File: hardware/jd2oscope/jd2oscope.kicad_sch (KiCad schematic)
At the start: 4 parts, among them U1 ESP32-DEVKITC-32D

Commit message: fix: ERC funtimes
fixed a bunch of dependencies with ERC checks for the schematic; shouuuuld be easier/actually possible to open on other devices now?? (added a buncha schematics & footprints to the local files & whatnot)
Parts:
- U1: footprint digikey-footprints:MODULE_ESP32-DEVKITC-32D -> pot:MODULE_ESP32-DEVKITC-32D; Availability (none) -> In Stock; Check_prices https://www.snapeda.com/parts/ESP32-DEVKITC-32D/Espressif+S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 -> https://www.snapeda.com/parts/ESP32-DevKitC-32D/Espressif+S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; Description_1 WiFi Development Tools (802.11) ESP32 General Development K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 -> ESP-WROOM-32 - Transceiver; 802.11 b/g/n (Wi-Fi, WiFi, WLAN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; MP ESP32-DEVKITC-32D -> ESP32-DevKitC-32D; Price (none) -> None; SnapEDA_Link https://www.snapeda.com/parts/ESP32-DEVKITC-32D/Espressif+S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 -> https://www.snapeda.com/parts/ESP32-DevKitC-32D/Espressif+S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
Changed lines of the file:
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@@
 			)
 		)
-		(property "Footprint" "digikey-footprints:MODULE_ESP32-DEVKITC-32D"
+		(property "Footprint" "pot:MODULE_ESP32-DEVKITC-32D"
 			(at 114.3 54.61 0)
 			(effects
@@
 			)
 		)
-		(property "SnapEDA_Link" "https://www.snapeda.com/parts/ESP32-DEVKITC-32D/Espressif+Systems/view-part/?ref=snap"
+		(property "SnapEDA_Link" "https://www.snapeda.com/parts/ESP32-DevKitC-32D/Espressif+Systems/view-part/?ref=snap"
 			(at 114.3 54.61 0)
 			(effects
@@
 			)
 		)
-		(property "Check_prices" "https://www.snapeda.com/parts/ESP32-DEVKITC-32D/Espressif+Systems/view-part/?ref=eda"
+		(property "Check_prices" "https://www.snapeda.com/parts/ESP32-DevKitC-32D/Espressif+Systems/view-part/?ref=eda"
 			(at 114.3 54.61 0)
 			(effects
@@
 			)
 		)
-		(property "MP" "ESP32-DEVKITC-32D"
-			(at 114.3 54.61 0)
-			(effects
-				(font
-					(size 1.27 1.27)
-				)
-				(justify bottom)
-				(hide yes)
-			)
-		)
-		(property "Description_1" "\n                        \n                            WiFi Development Tools (802.11) ESP32 General Development Kit, ESP32-WROOM-32D on the board\n                        \n"
+		(property "MP" "ESP32-DevKitC-32D"
+			(at 114.3 54.61 0)
+			(effects
+				(font
+					(size 1.27 1.27)
+				)
+				(justify bottom)
+				(hide yes)
+			)
+		)
+		(property "Description_1" "\n                        \n                            ESP-WROOM-32 - Transceiver; 802.11 b/g/n (Wi-Fi, WiFi, WLAN), Bluetooth® Smart Ready 4.x Dual Mode (BLE) 2.4GHz Evaluation Board\n                        \n"
 			(at 114.3 54.61 0)
 			(effects
@@
 				(hide yes)
 			)
+		)
+		(property "Price" "None"
+			(at 114.3 54.61 0)
+			(effects
+				(font
+					(size 1.27 1.27)
+				)
+				(justify bottom)
+				(hide yes)
+			)
+		)
+		(property "Availability" "In Stock"
+			(at 114.3 54.61 0)
+			(effects
+				(font
+					(size 1.27 1.27)
+				)
+				(justify bottom)
+				(hide yes)
+			)

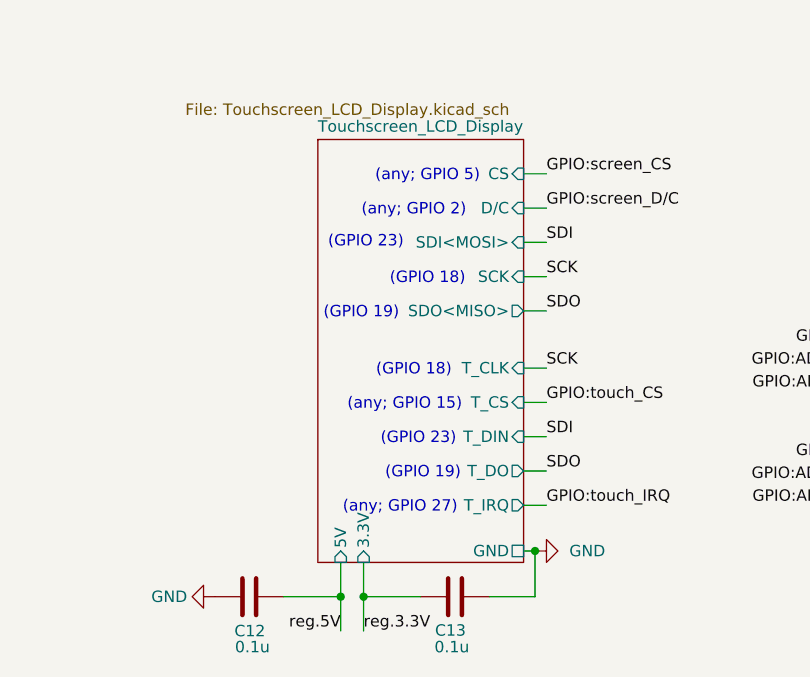
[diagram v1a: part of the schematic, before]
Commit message: feat: ERC is now happy!
We now pass all ERC checks in terms of errors; it is now fully satisfied!! (and, any warnings are just due to the fact that we made local edits to global symbol values, so we're ballin' all the way frfr)
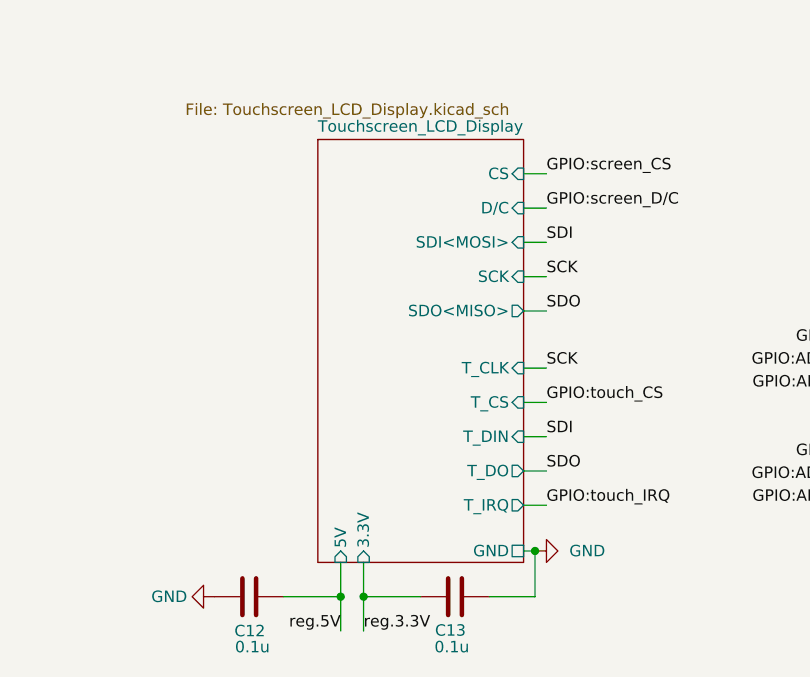
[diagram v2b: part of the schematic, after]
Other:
- note removed: "(GPIO 18)"
- note removed: "(GPIO 19)"
- note removed: "(GPIO 23)"
- note removed: "(any; GPIO 15)"
- note removed: "(any; GPIO 2)"
- note removed: "(any; GPIO 27)"
- note removed: "(any; GPIO 5)"
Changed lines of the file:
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@@
-		)
-	)
-	(text "(any; GPIO 27)"
-		(exclude_from_sim no)
-		(at 42.164 152.654 0)
-		(effects
-			(font
-				(size 1.27 1.27)
-			)
-		)
-	)
-	(text "(GPIO 23)"
-		(exclude_from_sim no)
-		(at 38.354 123.19 0)
-		(effects
-			(font
-				(size 1.27 1.27)
-			)
-		)
-	)
-	(text "(any; GPIO 5)"
-		(exclude_from_sim no)
-		(at 45.212 115.824 0)
-		(effects
-			(font
-				(size 1.27 1.27)
-			)
-		)
-	)
-	(text "(GPIO 18)"
-		(exclude_from_sim no)
-		(at 43.688 137.414 0)
-		(effects
-			(font
-				(size 1.27 1.27)
-			)
 		)
 	)
@@
 		)
 	)
-	(text "(any; GPIO 15)"
-		(exclude_from_sim no)
-		(at 42.672 141.224 0)
-		(effects
-			(font
-				(size 1.27 1.27)
-			)
-		)
-	)
-	(text "(GPIO 23)"
-		(exclude_from_sim no)
-		(at 44.196 145.034 0)
-		(effects
-			(font
-				(size 1.27 1.27)
-			)
-		)
-	)
-	(text "(GPIO 18)"
-		(exclude_from_sim no)
-		(at 45.212 127.254 0)
-		(effects
-			(font
-				(size 1.27 1.27)
-			)
-		)
-	)
 	(text "ESP32 ToDo:\n- [*] implement touchscreen wiring\n\n- [*] implement 5V_Regulator\n  - [*] PowerSwitch module between regulator output & reg.5V\n        (for toggling reg.5V to all dependent perip.s (i.e. turning device on/off)\n\n- [*] modules completed for:\n  - [*] pot.s\n  - [*] buttons\n    - [*] created \"signalInterfaceModule\"; has all req. buttons/pot.s to fully\n          control 1x signal (like a \"package\" that has everything we need for e/a\n          signal BNC connection)\n\n- [*] implement SignalInterpreterModule\n  - [*] figure out what the CONVST & EOC/INT pins are for\n  - [*] wire SPI comms. (for comm. w/ the ADC to recieve signal data in digital format)\n  - [*] update BNC footprint to new version (ref. text chat for link to it)\n  - [*] wire it all up relative to the rest of the circuit (sans finalized \"unique GPIO pins\"; still add e/a to the table though)\n\nmisc:\n- [ ] at end: GPIO pins arbitrarily assigned to GPIO locations on STM32 board\n  - [ ] Label connections on the GPIO \"Coding QOL\" table as well\n- [ ] check all sheets to make sure all pins labels are imported b4 moving on\n- [*] ensure that 0.1uF caps are added to e/a supply (& 10uF where needed too (47uF as well??))"
 		(exclude_from_sim no)
@@
 		)
 	)
-	(text "(any; GPIO 2)"
-		(exclude_from_sim no)
-		(at 43.688 119.634 0)
-		(effects
-			(font
-				(size 1.27 1.27)
-			)
-		)
-	)
-	(text "(GPIO 19)"
-		(exclude_from_sim no)
-		(at 37.846 131.064 0)
-		(effects
-			(font
-				(size 1.27 1.27)
-			)
-		)
-	)
 	(text "Note:\nwroom32 already has onboard\ndecopling cap for reg.3.3V\n(no need to add!)"
 		(exclude_from_sim no)
@@
 			)
 			(justify left)
-		)
-	)
-	(text "(GPIO 19)"
-		(exclude_from_sim no)
-		(at 44.704 148.844 0)
-		(effects
-			(font
-				(size 1.27 1.27)
-			)
 		)
 	)
@@
 			)
 		)
+		(pin "SDI<MOSI>" input
+			(at 55.88 123.19 0)
+			(effects
+				(font
+					(size 1.27 1.27)
+				)
+				(justify right)
+			)
+		)
+		(pin "SDO<MISO>" output
+			(at 55.88 130.81 0)
+			(effects
+				(font
+					(size 1.27 1.27)
+				)
+				(justify right)
+			)
+		)
+		(pin "5V" input
+			(at 35.56 158.75 270)
+			(effects
+				(font
+					(size 1.27 1.27)
+				)
+				(justify left)
+			)
+		)
+		(pin "T_CLK" input
+			(at 55.88 137.16 0)
+			(effects
+				(font
+					(size 1.27 1.27)
+				)
+				(justify right)
+			)
+		)
+		(pin "T_CS" input
+			(at 55.88 140.97 0)
+			(effects
+				(font
+					(size 1.27 1.27)
+				)
+				(justify right)
+			)
+		)
+		(pin "T_DIN" input
+			(at 55.88 144.78 0)
+			(effects
+				(font
+					(size 1.27 1.27)
+				)
+				(justify right)
+			)
+		)
+		(pin "T_DO" output
+			(at 55.88 148.59 0)
+			(effects
+				(font
+					(size 1.27 1.27)
+				)
+				(justify right)
+			)
+		)
+		(pin "T_IRQ" output
+			(at 55.88 152.4 0)
+			(effects
+				(font
+					(size 1.27 1.27)
+				)
+				(justify right)
+			)
+		)
+		(pin "GND" passive
+			(at 55.88 157.48 0)
+			(effects
+				(font
+					(size 1.27 1.27)
+				)
+				(justify right)
+			)
+		)
 		(pin "3.3V" input
 			(at 38.1 158.75 270)
@@
 			)
 		)
-		(pin "SDI<MOSI>" input
-			(at 55.88 123.19 0)
-			(effects
-				(font
-					(size 1.27 1.27)
-				)
-				(justify right)
-			)
-		)
-		(pin "SDO<MISO>" output
-			(at 55.88 130.81 0)
-			(effects
-				(font
-					(size 1.27 1.27)
-				)
-				(justify right)
-			)
-		)
-		(pin "5V" input
-			(at 35.56 158.75 270)
-			(effects
-				(font
-					(size 1.27 1.27)
-				)
-				(justify left)
-			)
-		)
-		(pin "T_CLK" input
-			(at 55.88 137.16 0)
-			(effects
-				(font
-					(size 1.27 1.27)
-				)
-				(justify right)
-			)
-		)
-		(pin "T_CS" input
-			(at 55.88 140.97 0)
-			(effects
-				(font
-					(size 1.27 1.27)
-				)
-				(justify right)
-			)
-		)
-		(pin "T_DIN" input
-			(at 55.88 144.78 0)
-			(effects
-				(font
-					(size 1.27 1.27)
-				)
-				(justify right)
-			)
-		)
-		(pin "T_DO" output
-			(at 55.88 148.59 0)
-			(effects
-				(font
-					(size 1.27 1.27)
-				)
-				(justify right)
-			)
-		)
-		(pin "T_IRQ" output
-			(at 55.88 152.4 0)
-			(effects
-				(font
-					(size 1.27 1.27)
-				)
-				(justify right)
-			)
-		)
-		(pin "GND" passive
-			(at 55.88 157.48 0)
-			(effects
-				(font
-					(size 1.27 1.27)
-				)
-				(justify right)
-			)
-		)

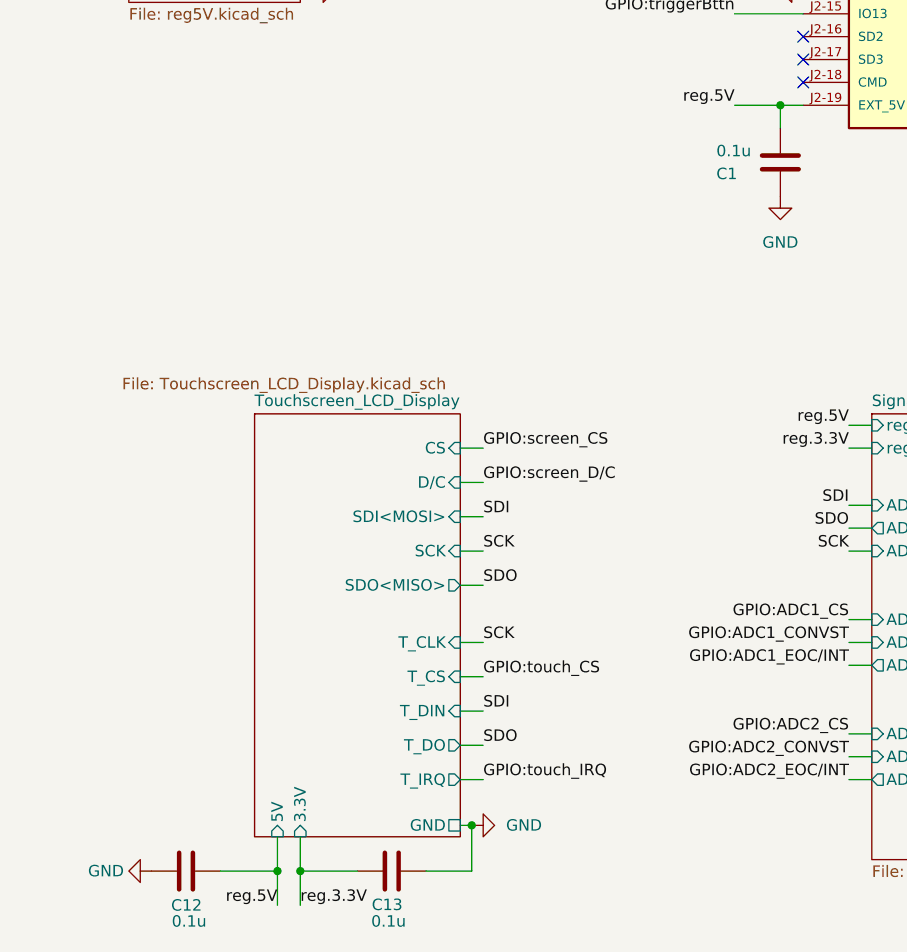
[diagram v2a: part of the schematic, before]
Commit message: feat/fix: no more errors for PCB import too!
Now both the ERC, and the schematic import (and my OCD) are completely satisfied, and we can dev the actual PCB; let's go!! :D
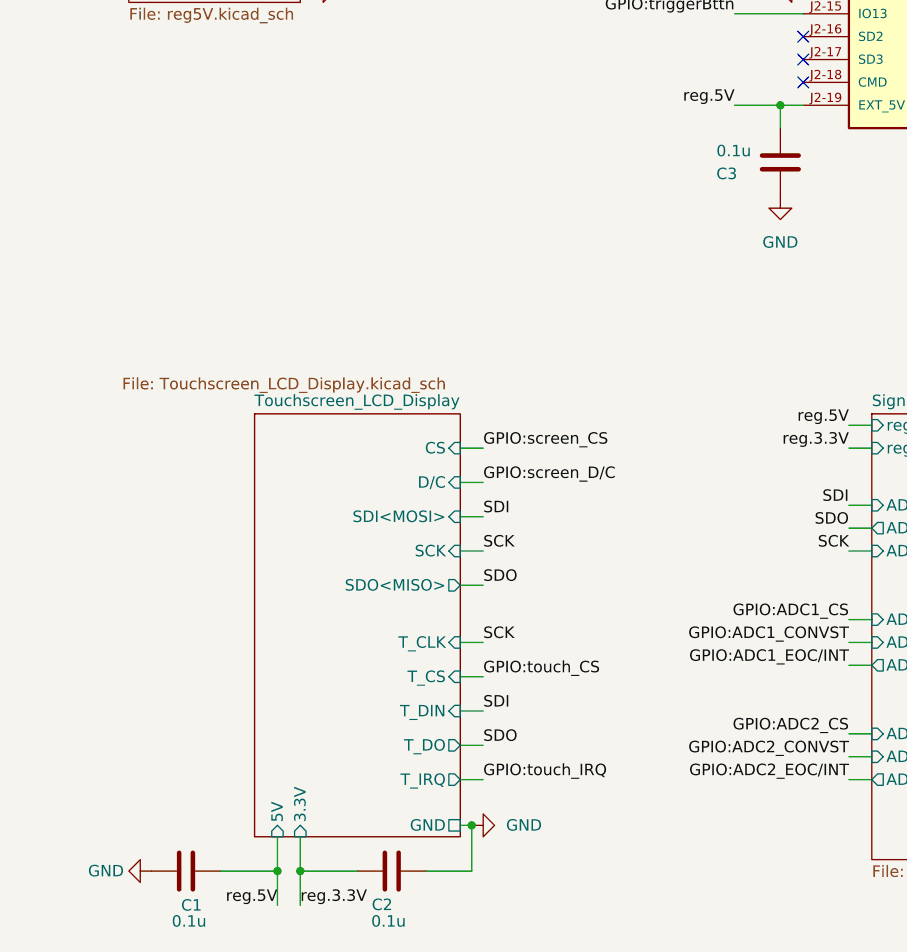
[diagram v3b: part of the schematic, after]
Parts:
- U1: footprint pot:MODULE_ESP32-DEVKITC-32D -> jd2Oscope_Footprints:MODULE_ESP32-DEVKITC-32D
- renumbered C12 to C1, C13 to C2, C1 to C3
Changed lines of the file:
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@@
 		(dnp no)
 		(fields_autoplaced yes)
-		(property "Reference" "#PWR01"
+		(property "Reference" "#PWR03"
 			(at 63.5 157.48 0)
 			(effects
@@
 			(project ""
 				(path "/eb18a3da-9fbf-4329-a814-1afab785c817"
-					(reference "#PWR01")
+					(reference "#PWR03")
 					(unit 1)
 				)
@@
 		(on_board yes)
 		(dnp no)
-		(property "Reference" "C13"
+		(property "Reference" "C2"
 			(at 46.0375 166.3064 90)
 			(effects
@@
 			(project "jd2oscope"
 				(path "/eb18a3da-9fbf-4329-a814-1afab785c817"
-					(reference "C13")
+					(reference "C2")
 					(unit 1)
 				)
@@
 		(dnp no)
 		(fields_autoplaced yes)
-		(property "Reference" "#PWR012"
+		(property "Reference" "#PWR05"
 			(at 87.63 64.77 0)
 			(effects
@@
 			(project "jd2oscope"
 				(path "/eb18a3da-9fbf-4329-a814-1afab785c817"
-					(reference "#PWR012")
+					(reference "#PWR05")
 					(unit 1)
 				)
@@
 		(dnp no)
 		(fields_autoplaced yes)
-		(property "Reference" "#PWR08"
+		(property "Reference" "#PWR07"
 			(at 140.97 46.99 0)
 			(effects
@@
 			(project ""
 				(path "/eb18a3da-9fbf-4329-a814-1afab785c817"
-					(reference "#PWR08")
+					(reference "#PWR07")
 					(unit 1)
 				)
@@
 		(dnp no)
 		(fields_autoplaced yes)
-		(property "Reference" "#PWR03"
+		(property "Reference" "#PWR02"
 			(at 45.72 64.77 0)
 			(effects
@@
 			(project ""
 				(path "/eb18a3da-9fbf-4329-a814-1afab785c817"
-					(reference "#PWR03")
+					(reference "#PWR02")
 					(unit 1)
 				)
@@
 		(dnp no)
 		(fields_autoplaced yes)
-		(property "Reference" "#PWR07"
+		(property "Reference" "#PWR04"
 			(at 91.44 93.98 0)
 			(effects
@@
 			(project "jd2oscope"
 				(path "/eb18a3da-9fbf-4329-a814-1afab785c817"
-					(reference "#PWR07")
+					(reference "#PWR04")
 					(unit 1)
 				)
@@
 		(dnp no)
 		(fields_autoplaced yes)
-		(property "Reference" "#PWR011"
+		(property "Reference" "#PWR06"
 			(at 140.97 31.75 0)
 			(effects
@@
 			(project "jd2oscope"
 				(path "/eb18a3da-9fbf-4329-a814-1afab785c817"
-					(reference "#PWR011")
+					(reference "#PWR06")
 					(unit 1)
 				)
@@
 		(on_board yes)
 		(dnp no)
-		(property "Reference" "C12"
+		(property "Reference" "C1"
 			(at 27.178 166.37 90)
 			(effects
@@
 			(project "jd2oscope"
 				(path "/eb18a3da-9fbf-4329-a814-1afab785c817"
-					(reference "C12")
+					(reference "C1")
 					(unit 1)
 				)
@@
 		(on_board yes)
 		(dnp no)
-		(property "Reference" "C1"
+		(property "Reference" "C3"
 			(at 84.328 85.09 0)
 			(effects
@@
 			(project "jd2oscope"
 				(path "/eb18a3da-9fbf-4329-a814-1afab785c817"
-					(reference "C1")
+					(reference "C3")
 					(unit 1)
 				)
@@
 			)
 		)
-		(property "Footprint" "pot:MODULE_ESP32-DEVKITC-32D"
+		(property "Footprint" "jd2Oscope_Footprints:MODULE_ESP32-DEVKITC-32D"
 			(at 114.3 54.61 0)
 			(effects
@@
 		(on_board yes)
 		(dnp no)
-		(property "Reference" "#PWR06"
+		(property "Reference" "#PWR01"
 			(at 15.24 162.56 0)
 			(effects
@@
 			(project "jd2oscope"
 				(path "/eb18a3da-9fbf-4329-a814-1afab785c817"
-					(reference "#PWR06")
+					(reference "#PWR01")
 					(unit 1)
 				)
@@
 		(dnp no)
 		(fields_autoplaced yes)
-		(property "Reference" "#PWR02"
+		(property "Reference" "#PWR08"
 			(at 151.13 160.02 0)
 			(effects
@@
 			(project ""
 				(path "/eb18a3da-9fbf-4329-a814-1afab785c817"
-					(reference "#PWR02")
+					(reference "#PWR08")
 					(unit 1)
 				)
